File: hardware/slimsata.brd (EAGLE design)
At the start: 20.3 x 54.6 mm, 2 parts, among them CON1 MOLEX_67492, CON2 MOLEX_47300

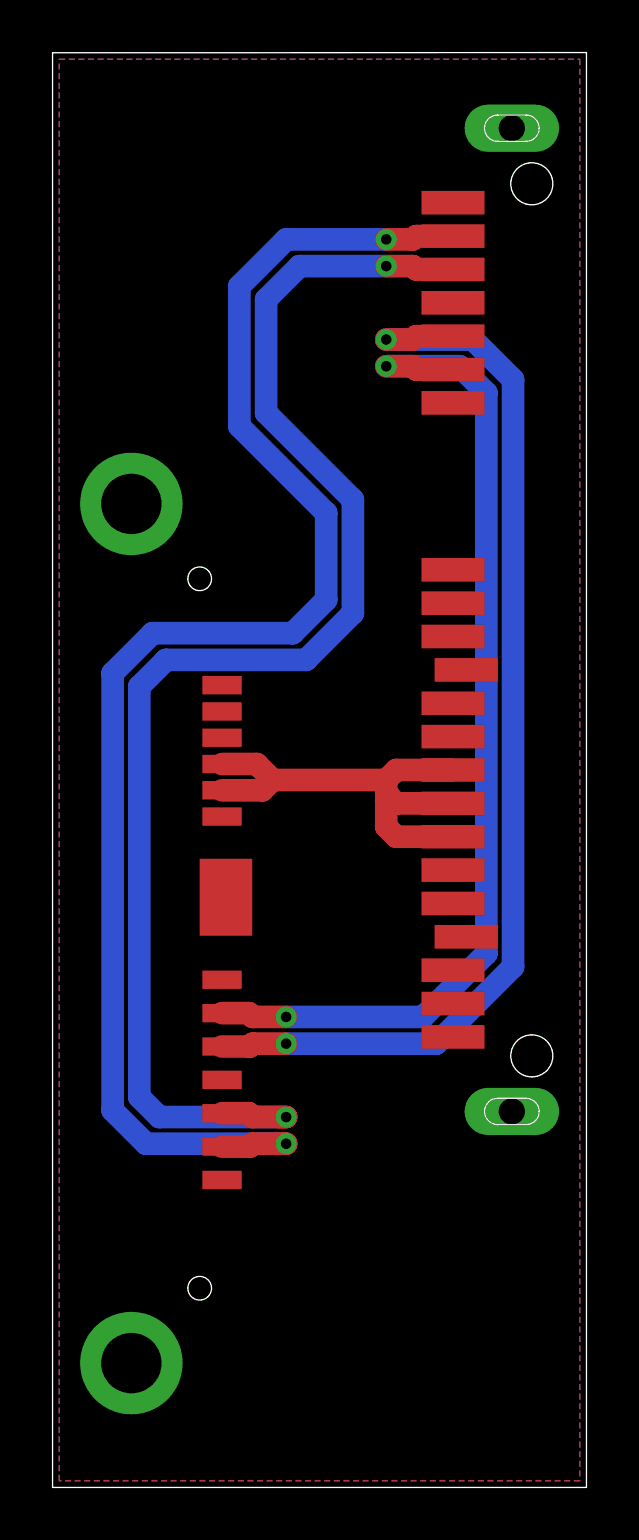
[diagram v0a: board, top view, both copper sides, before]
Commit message: Längenanpassung
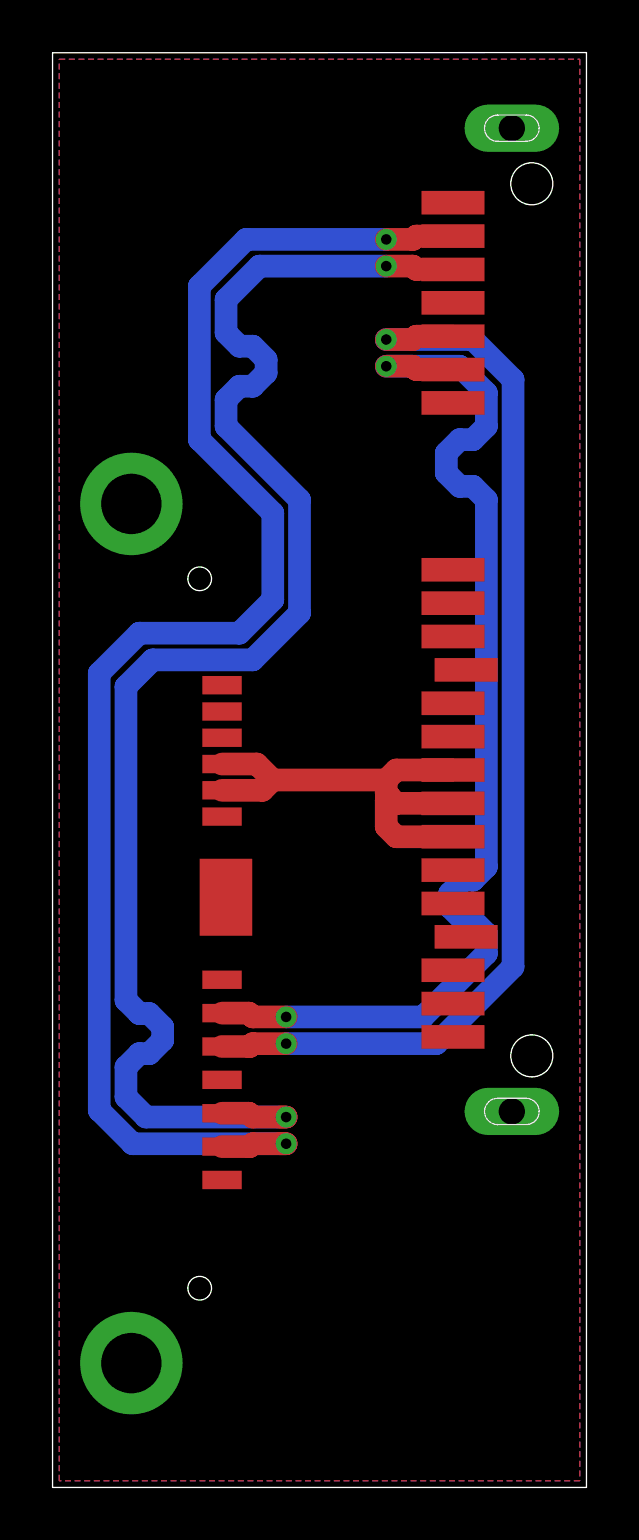
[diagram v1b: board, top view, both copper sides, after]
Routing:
- net N$6: track 54.6 -> 58.3 mm
- net N$8: track 39.3 -> 42.7 mm
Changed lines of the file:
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@@
 <wire x1="13.716" y1="47.498" x2="12.7" y2="47.498" width="0.8636" layer="1"/>
 <via x="12.7" y="47.498" extent="1-16" drill="0.4"/>
-<wire x1="12.7" y1="47.498" x2="8.89" y2="47.498" width="0.8636" layer="16"/>
-<wire x1="8.89" y1="47.498" x2="7.112" y2="45.72" width="0.8636" layer="16"/>
-<wire x1="7.112" y1="45.72" x2="7.112" y2="40.386" width="0.8636" layer="16"/>
-<wire x1="7.112" y1="40.386" x2="10.414" y2="37.084" width="0.8636" layer="16"/>
-<wire x1="10.414" y1="37.084" x2="10.414" y2="33.782" width="0.8636" layer="16"/>
-<wire x1="10.414" y1="33.782" x2="9.144" y2="32.512" width="0.8636" layer="16"/>
-<wire x1="9.144" y1="32.512" x2="3.81" y2="32.512" width="0.8636" layer="16"/>
-<wire x1="3.81" y1="32.512" x2="2.286" y2="30.988" width="0.8636" layer="16"/>
-<wire x1="2.286" y1="30.988" x2="2.286" y2="14.351" width="0.8636" layer="16"/>
-<wire x1="2.286" y1="14.351" x2="3.556" y2="13.081" width="0.8636" layer="16"/>
-<wire x1="3.556" y1="13.081" x2="8.89" y2="13.081" width="0.8636" layer="16"/>
+<wire x1="12.7" y1="47.498" x2="7.366" y2="47.498" width="0.8636" layer="16"/>
+<wire x1="7.366" y1="47.498" x2="5.588" y2="45.72" width="0.8636" layer="16"/>
+<wire x1="5.588" y1="39.878" x2="5.588" y2="45.72" width="0.8636" layer="16"/>
+<wire x1="5.588" y1="39.878" x2="8.382" y2="37.084" width="0.8636" layer="16"/>
+<wire x1="8.382" y1="37.084" x2="8.382" y2="33.782" width="0.8636" layer="16"/>
+<wire x1="8.382" y1="33.782" x2="7.112" y2="32.512" width="0.8636" layer="16"/>
+<wire x1="7.112" y1="32.512" x2="3.302" y2="32.512" width="0.8636" layer="16"/>
+<wire x1="3.302" y1="32.512" x2="1.778" y2="30.988" width="0.8636" layer="16"/>
+<wire x1="1.778" y1="30.988" x2="1.778" y2="14.351" width="0.8636" layer="16"/>
+<wire x1="1.778" y1="14.351" x2="3.048" y2="13.081" width="0.8636" layer="16"/>
+<wire x1="3.048" y1="13.081" x2="8.89" y2="13.081" width="0.8636" layer="16"/>
 <via x="8.89" y="13.081" extent="1-16" drill="0.4"/>
 <wire x1="8.89" y1="13.081" x2="8.636" y2="13.081" width="0.8636" layer="1"/>
@@
 <wire x1="13.716" y1="46.482" x2="12.7" y2="46.482" width="0.8636" layer="1"/>
 <via x="12.7" y="46.482" extent="1-16" drill="0.4"/>
-<wire x1="12.7" y1="46.482" x2="9.398" y2="46.482" width="0.8636" layer="16"/>
-<wire x1="9.398" y1="46.482" x2="8.128" y2="45.212" width="0.8636" layer="16"/>
-<wire x1="8.128" y1="45.212" x2="8.128" y2="40.894" width="0.8636" layer="16"/>
-<wire x1="8.128" y1="40.894" x2="11.43" y2="37.592" width="0.8636" layer="16"/>
-<wire x1="11.43" y1="37.592" x2="11.43" y2="33.274" width="0.8636" layer="16"/>
-<wire x1="11.43" y1="33.274" x2="9.652" y2="31.496" width="0.8636" layer="16"/>
-<wire x1="9.652" y1="31.496" x2="4.318" y2="31.496" width="0.8636" layer="16"/>
-<wire x1="4.318" y1="31.496" x2="3.302" y2="30.48" width="0.8636" layer="16"/>
-<wire x1="3.302" y1="30.48" x2="3.302" y2="14.859" width="0.8636" layer="16"/>
-<wire x1="3.302" y1="14.859" x2="4.064" y2="14.097" width="0.8636" layer="16"/>
-<wire x1="4.064" y1="14.097" x2="8.89" y2="14.097" width="0.8636" layer="16"/>
+<wire x1="12.7" y1="46.482" x2="7.874" y2="46.482" width="0.8636" layer="16"/>
+<wire x1="7.874" y1="46.482" x2="6.604" y2="45.212" width="0.8636" layer="16"/>
+<wire x1="6.604" y1="45.212" x2="6.604" y2="43.942" width="0.8636" layer="16"/>
+<wire x1="6.604" y1="43.942" x2="7.112" y2="43.434" width="0.8636" layer="16"/>
+<wire x1="7.112" y1="43.434" x2="7.62" y2="43.434" width="0.8636" layer="16"/>
+<wire x1="7.62" y1="43.434" x2="8.128" y2="42.926" width="0.8636" layer="16"/>
+<wire x1="8.128" y1="42.926" x2="8.128" y2="42.418" width="0.8636" layer="16"/>
+<wire x1="8.128" y1="42.418" x2="7.62" y2="41.91" width="0.8636" layer="16"/>
+<wire x1="7.62" y1="41.91" x2="7.112" y2="41.91" width="0.8636" layer="16"/>
+<wire x1="7.112" y1="41.91" x2="6.604" y2="41.402" width="0.8636" layer="16"/>
+<wire x1="6.604" y1="41.402" x2="6.604" y2="40.386" width="0.8636" layer="16"/>
+<wire x1="6.604" y1="40.386" x2="9.398" y2="37.592" width="0.8636" layer="16"/>
+<wire x1="9.398" y1="37.592" x2="9.398" y2="33.274" width="0.8636" layer="16"/>
+<wire x1="9.398" y1="33.274" x2="7.62" y2="31.496" width="0.8636" layer="16"/>
+<wire x1="7.62" y1="31.496" x2="3.81" y2="31.496" width="0.8636" layer="16"/>
+<wire x1="3.81" y1="31.496" x2="2.794" y2="30.48" width="0.8636" layer="16"/>
+<wire x1="2.794" y1="18.542" x2="2.794" y2="30.48" width="0.8636" layer="16"/>
+<wire x1="2.794" y1="18.542" x2="3.302" y2="18.034" width="0.8636" layer="16"/>
+<wire x1="3.302" y1="18.034" x2="3.683" y2="18.034" width="0.8636" layer="16"/>
+<wire x1="3.683" y1="18.034" x2="4.191" y2="17.526" width="0.8636" layer="16"/>
+<wire x1="4.191" y1="17.526" x2="4.191" y2="17.018" width="0.8636" layer="16"/>
+<wire x1="4.191" y1="17.018" x2="3.683" y2="16.51" width="0.8636" layer="16"/>
+<wire x1="3.683" y1="16.51" x2="3.302" y2="16.51" width="0.8636" layer="16"/>
+<wire x1="3.302" y1="16.51" x2="2.794" y2="16.002" width="0.8636" layer="16"/>
+<wire x1="2.794" y1="16.002" x2="2.794" y2="14.859" width="0.8636" layer="16"/>
+<wire x1="2.794" y1="14.859" x2="3.556" y2="14.097" width="0.8636" layer="16"/>
+<wire x1="3.556" y1="14.097" x2="8.89" y2="14.097" width="0.8636" layer="16"/>
 <via x="8.89" y="14.097" extent="1-16" drill="0.4"/>
 <wire x1="8.89" y1="14.097" x2="8.636" y2="14.097" width="0.8636" layer="1"/>
@@
 <wire x1="12.7" y1="42.672" x2="15.494" y2="42.672" width="0.8636" layer="16"/>
 <wire x1="15.494" y1="42.672" x2="16.51" y2="41.656" width="0.8636" layer="16"/>
-<wire x1="16.51" y1="41.656" x2="16.51" y2="20.32" width="0.8636" layer="16"/>
+<wire x1="16.51" y1="41.656" x2="16.51" y2="40.386" width="0.8636" layer="16"/>
+<wire x1="16.51" y1="40.386" x2="16.002" y2="39.878" width="0.8636" layer="16"/>
+<wire x1="15.494" y1="39.878" x2="16.002" y2="39.878" width="0.8636" layer="16"/>
+<wire x1="15.494" y1="39.878" x2="14.986" y2="39.37" width="0.8636" layer="16"/>
+<wire x1="14.986" y1="39.37" x2="14.986" y2="38.608" width="0.8636" layer="16"/>
+<wire x1="14.986" y1="38.608" x2="15.494" y2="38.1" width="0.8636" layer="16"/>
+<wire x1="15.494" y1="38.1" x2="16.002" y2="38.1" width="0.8636" layer="16"/>
+<wire x1="16.002" y1="38.1" x2="16.51" y2="37.592" width="0.8636" layer="16"/>
+<wire x1="16.51" y1="37.592" x2="16.51" y2="23.622" width="0.8636" layer="16"/>
+<wire x1="16.002" y1="23.114" x2="16.51" y2="23.622" width="0.8636" layer="16"/>
+<wire x1="16.002" y1="23.114" x2="15.621" y2="23.114" width="0.8636" layer="16"/>
+<wire x1="15.621" y1="23.114" x2="15.113" y2="22.606" width="0.8636" layer="16"/>
+<wire x1="15.113" y1="22.606" x2="15.113" y2="22.098" width="0.8636" layer="16"/>
+<wire x1="15.113" y1="22.098" x2="15.621" y2="21.59" width="0.8636" layer="16"/>
+<wire x1="15.621" y1="21.59" x2="16.002" y2="21.59" width="0.8636" layer="16"/>
+<wire x1="16.002" y1="21.59" x2="16.51" y2="21.082" width="0.8636" layer="16"/>
+<wire x1="16.51" y1="21.082" x2="16.51" y2="20.32" width="0.8636" layer="16"/>
 <wire x1="16.51" y1="20.32" x2="14.097" y2="17.907" width="0.8636" layer="16"/>
 <wire x1="14.097" y1="17.907" x2="8.89" y2="17.907" width="0.8636" layer="16"/>
@@
 </signal>
 <signal name="GND" class="2">
-<contactref element="CON2" pad="S1"/>
-<contactref element="CON1" pad="S1"/>
-<contactref element="CON1" pad="S4"/>
-<contactref element="CON2" pad="S4"/>
-<contactref element="CON1" pad="S7"/>
-<contactref element="CON2" pad="S7"/>
 <contactref element="CON1" pad="MECH2"/>
 <contactref element="CON1" pad="MECH1"/>
@@
 <vertex x="0.254" y="0.254"/>
 </polygon>
+<contactref element="CON2" pad="S1"/>
+<contactref element="CON1" pad="S1"/>
+<contactref element="CON1" pad="S4"/>
+<contactref element="CON2" pad="S4"/>
+<contactref element="CON1" pad="S7"/>
+<contactref element="CON2" pad="S7"/>
 </signal>
 </signals>

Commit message: kleine Änderungen
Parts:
- CON2: device sata:MOLEX_47300-1005 -> sata:MOLEX_47300-100X/101X
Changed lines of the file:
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@@
 <elements>
 <element name="CON1" library="sata" package="MOLEX_67492" value="MOLEX_67492" x="20.32" y="33.02" rot="R90"/>
-<element name="CON2" library="sata" package="MOLEX_47300-1005" value="MOLEX_47300" x="0" y="21.082" rot="R270"/>
+<element name="CON2" library="sata" package="MOLEX_47300-100X/101X" value="MOLEX_47300" x="0" y="21.082" rot="R270"/>
 </elements>
 <signals>
@@
 <wire x1="5.588" y1="39.878" x2="5.588" y2="45.72" width="0.8636" layer="16"/>
 <wire x1="5.588" y1="39.878" x2="8.382" y2="37.084" width="0.8636" layer="16"/>
-<wire x1="8.382" y1="37.084" x2="8.382" y2="33.782" width="0.8636" layer="16"/>
-<wire x1="8.382" y1="33.782" x2="7.112" y2="32.512" width="0.8636" layer="16"/>
-<wire x1="7.112" y1="32.512" x2="3.302" y2="32.512" width="0.8636" layer="16"/>
-<wire x1="3.302" y1="32.512" x2="1.778" y2="30.988" width="0.8636" layer="16"/>
-<wire x1="1.778" y1="30.988" x2="1.778" y2="14.351" width="0.8636" layer="16"/>
+<wire x1="8.382" y1="37.084" x2="8.382" y2="33.528" width="0.8636" layer="16"/>
+<wire x1="8.382" y1="33.528" x2="7.112" y2="32.258" width="0.8636" layer="16"/>
+<wire x1="7.112" y1="32.258" x2="3.302" y2="32.258" width="0.8636" layer="16"/>
+<wire x1="3.302" y1="32.258" x2="1.778" y2="30.734" width="0.8636" layer="16"/>
+<wire x1="1.778" y1="30.734" x2="1.778" y2="14.351" width="0.8636" layer="16"/>
 <wire x1="1.778" y1="14.351" x2="3.048" y2="13.081" width="0.8636" layer="16"/>
 <wire x1="3.048" y1="13.081" x2="8.89" y2="13.081" width="0.8636" layer="16"/>
@@
 <wire x1="6.604" y1="41.402" x2="6.604" y2="40.386" width="0.8636" layer="16"/>
 <wire x1="6.604" y1="40.386" x2="9.398" y2="37.592" width="0.8636" layer="16"/>
-<wire x1="9.398" y1="37.592" x2="9.398" y2="33.274" width="0.8636" layer="16"/>
-<wire x1="9.398" y1="33.274" x2="7.62" y2="31.496" width="0.8636" layer="16"/>
-<wire x1="7.62" y1="31.496" x2="3.81" y2="31.496" width="0.8636" layer="16"/>
-<wire x1="3.81" y1="31.496" x2="2.794" y2="30.48" width="0.8636" layer="16"/>
-<wire x1="2.794" y1="18.542" x2="2.794" y2="30.48" width="0.8636" layer="16"/>
+<wire x1="9.398" y1="37.592" x2="9.398" y2="33.02" width="0.8636" layer="16"/>
+<wire x1="9.398" y1="33.02" x2="7.62" y2="31.242" width="0.8636" layer="16"/>
+<wire x1="7.62" y1="31.242" x2="3.81" y2="31.242" width="0.8636" layer="16"/>
+<wire x1="3.81" y1="31.242" x2="2.794" y2="30.226" width="0.8636" layer="16"/>
+<wire x1="2.794" y1="18.542" x2="2.794" y2="30.226" width="0.8636" layer="16"/>
 <wire x1="2.794" y1="18.542" x2="3.302" y2="18.034" width="0.8636" layer="16"/>
 <wire x1="3.302" y1="18.034" x2="3.683" y2="18.034" width="0.8636" layer="16"/>

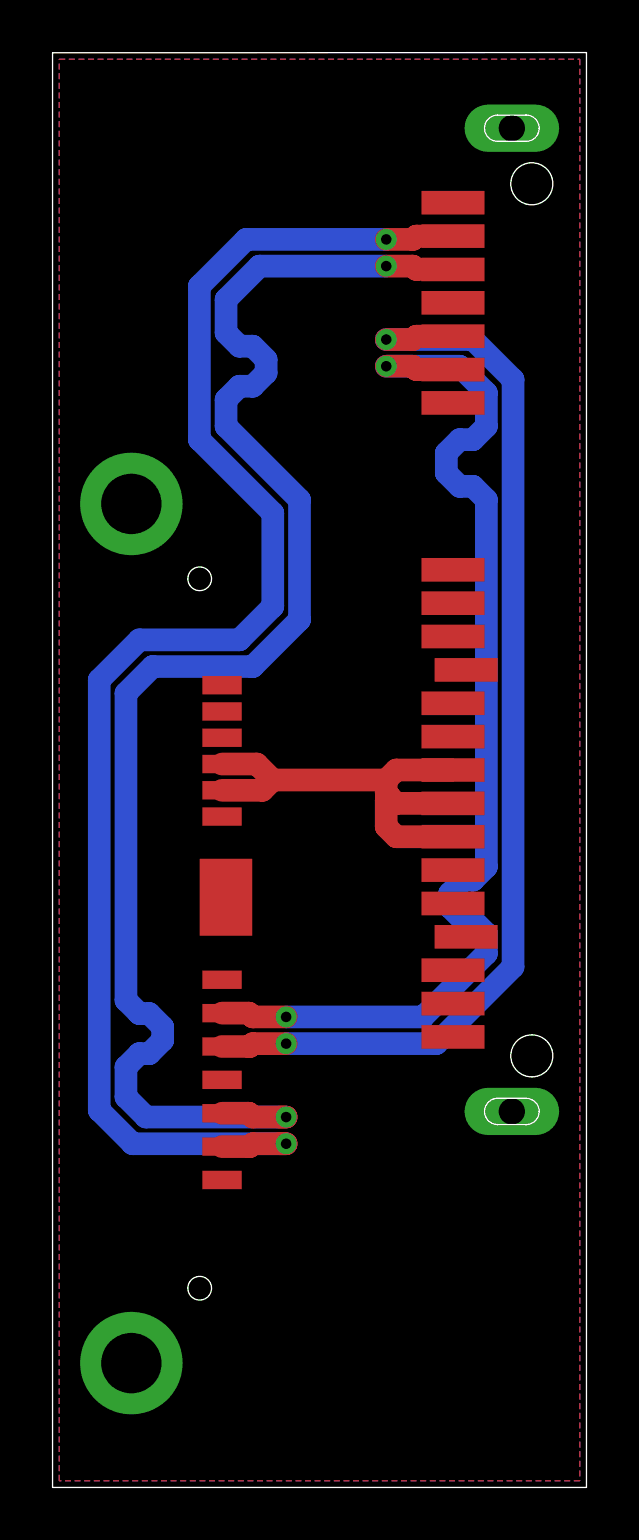
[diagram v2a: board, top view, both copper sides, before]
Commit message: signals routed as differential pair without length matching
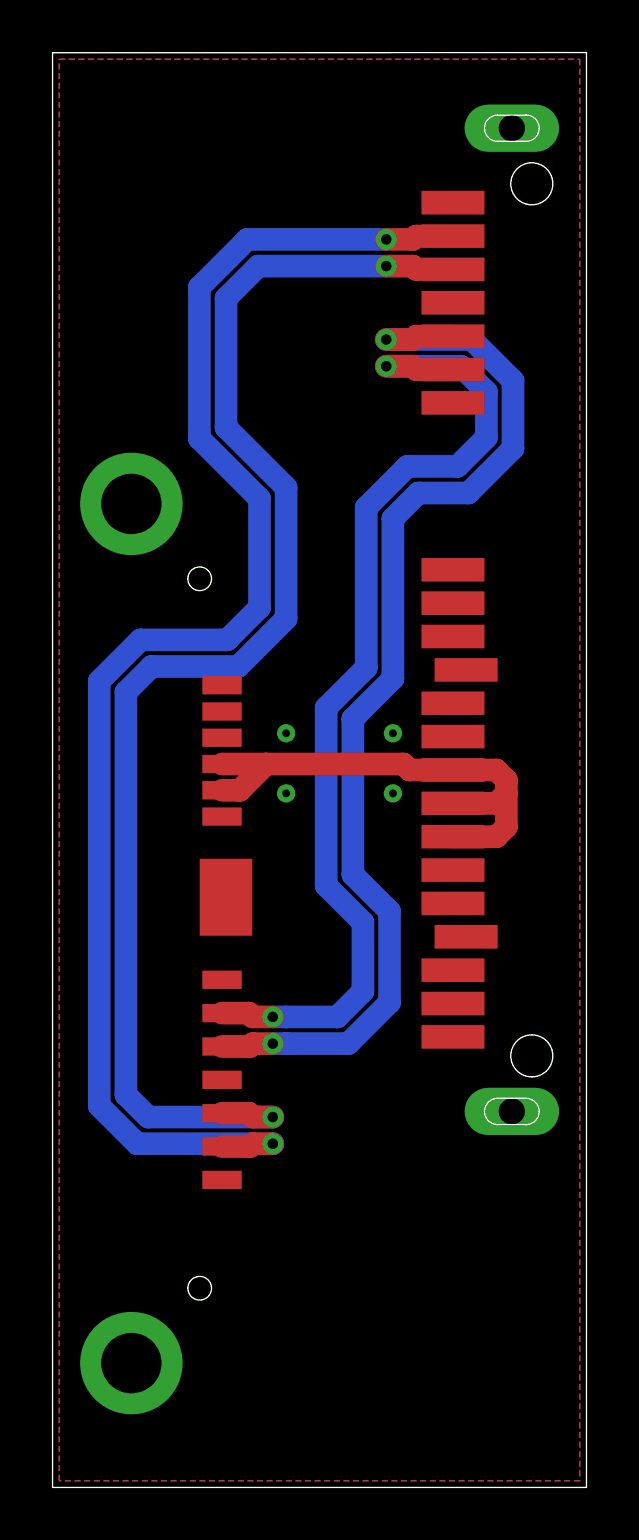
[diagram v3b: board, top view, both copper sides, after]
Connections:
- net N$5 renamed A_P
- net N$6 renamed A_N
- net N$7 renamed B_N
- net N$8 renamed B_P
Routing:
- net A_N: track 58.3 -> 52.9 mm
- net B_P: track 42.7 -> 39.7 mm
- net A_P: track 58.3 -> 56.2 mm
- net N$3: track 18.4 -> 19.3 mm
